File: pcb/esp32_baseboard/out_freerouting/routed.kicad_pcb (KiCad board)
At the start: 2 copper layers, 235 x 132 mm, 42 parts, among them J1 Screw_12V_IN, J10 LIM_MIN_NC, J11 LIM_MAX_NC, J12 LIM_MIN_NC, J13 LIM_MAX_NC, J14 BUP_30S, J15 BUZZER_5V, J16 AOD4184, J17 TFT_TOUCH, J18 EC11_ENC, J2 NEMA17_OUT, J4 OPTO_FIELD_IN, J5 GA12_N20, J6 GA12_N20, J7 GA12_N20, J8 LIM_MIN_NC, J9 LIM_MAX_NC, U1 ESP32_S3_DevKitC_1, U2 MP1584_5V3A, U3 TMC2209, U4 PC817_4CH, U5 DRV8871_Module, U6 DRV8871_Module, U7 DRV8871_Module, U9 PC817_4CH

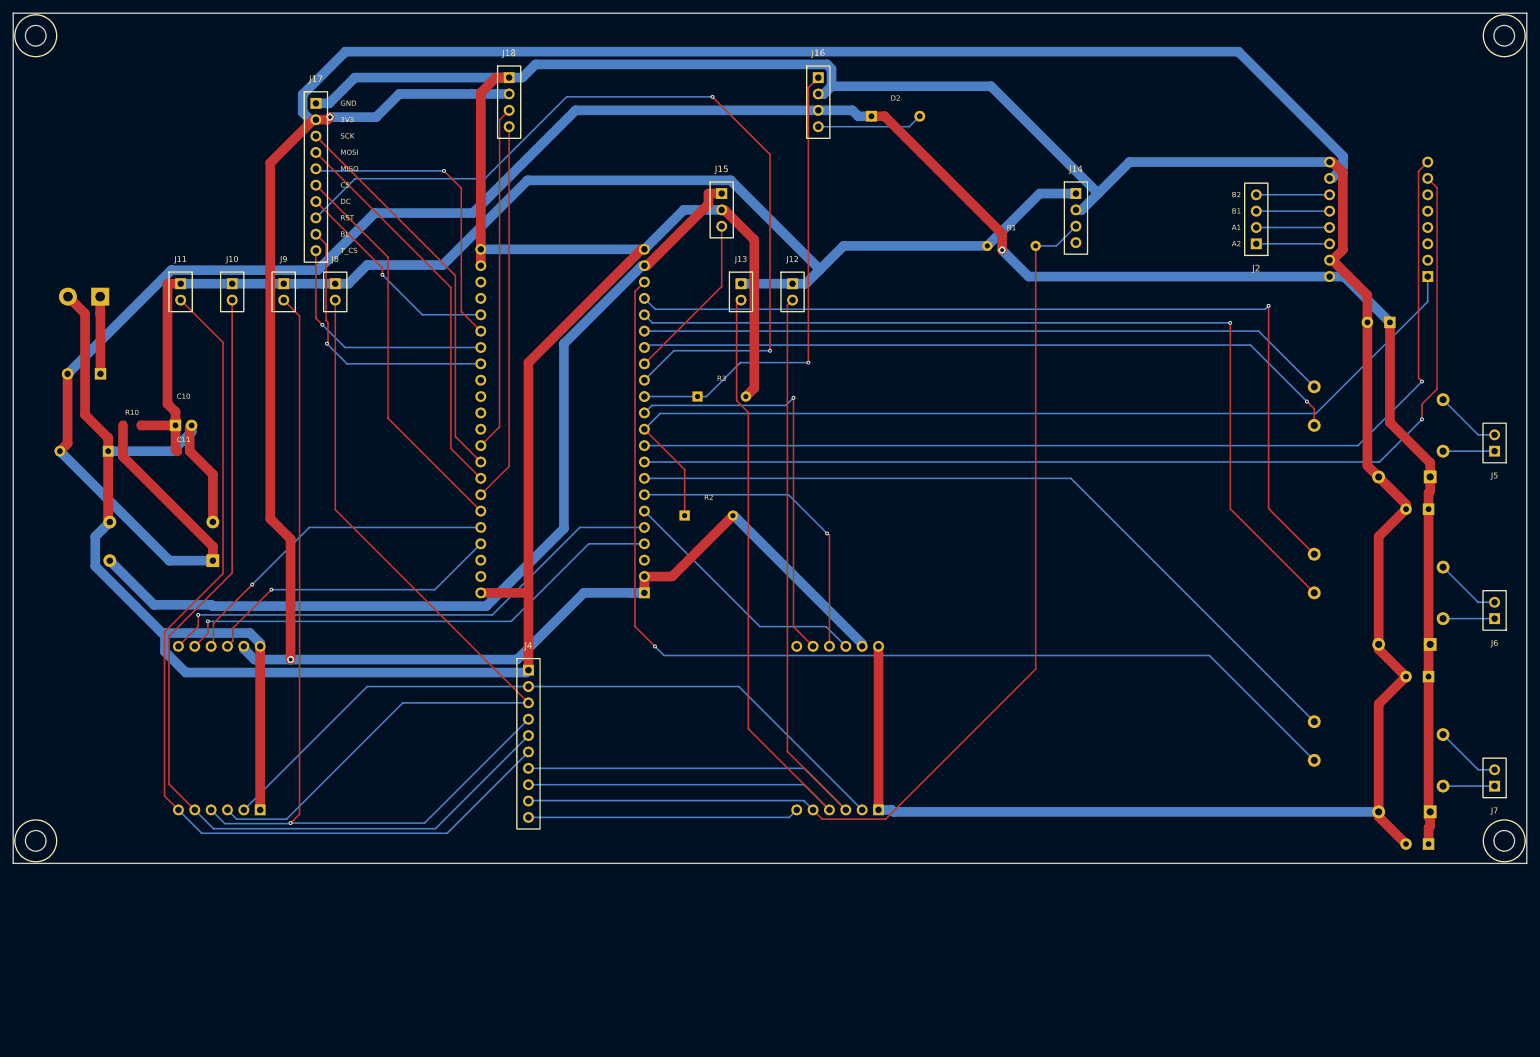
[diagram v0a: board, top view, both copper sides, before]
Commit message: sắp xếp và chọn lại linh kiện cho PCB
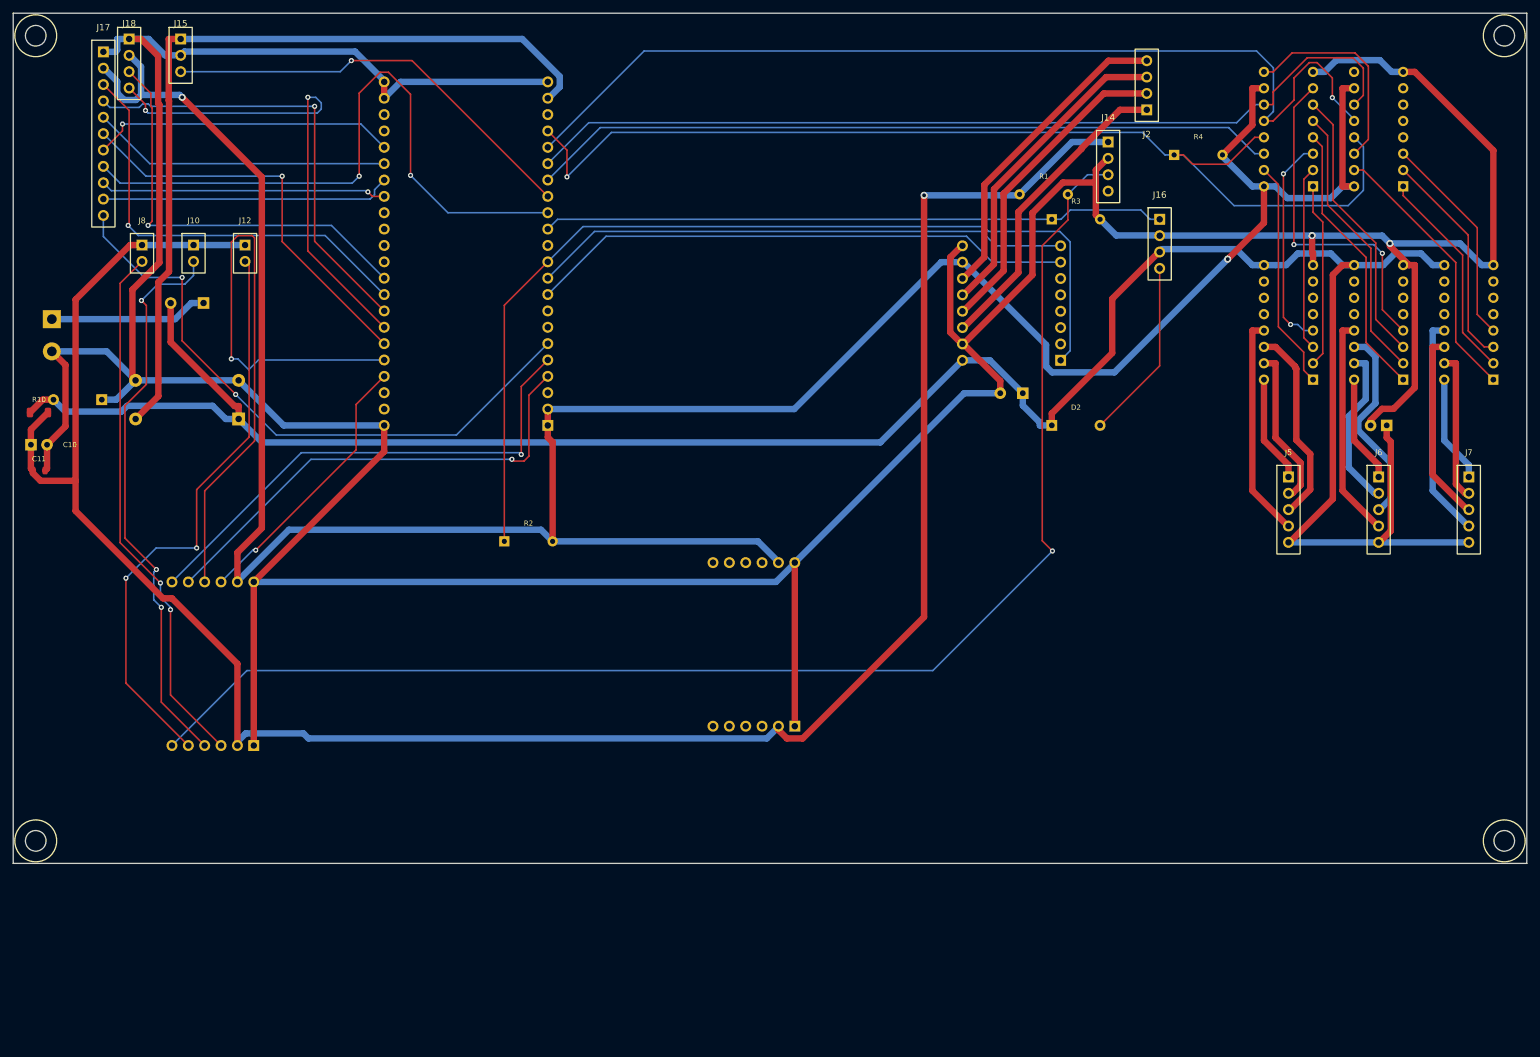
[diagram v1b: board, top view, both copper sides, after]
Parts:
- removed C22, C23: 470u/25V, ESP32_Carrier:CP_Radial_D8_470u_25V
- removed J11, J13, J9: LIM_MAX_NC, ESP32_Carrier:PinHeader_1x02_LimitSW
- removed J4: OPTO_FIELD_IN, ESP32_Carrier:PinHeader_1x10_OptoField
- added R4: 10k, ESP32_Carrier:R_Axial_4k7_BUP, F.Cu at (219.0, 52.0)
- added U10: 74HC595, ESP32_Carrier:74HC595, B.Cu at (233.0, 48.0)
- added U11: 74HC595, ESP32_Carrier:74HC595, B.Cu at (247.0, 48.0)
- C21: value 470u/25V -> 100u/25V; footprint ESP32_Carrier:CP_Radial_D8_470u_25V -> ESP32_Carrier:CP_Radial_D6_100u_25V
- J10: value LIM_MIN_NC -> LIM_HOME2
- J12: value LIM_MIN_NC -> LIM_HOME3
- J17: footprint ESP32_Carrier:PinHeader_1x10_TFT -> ESP32_Carrier:PinHeader_1x11_TFT
- J5, J6, J7: value GA12_N20 -> 28BYJ48; footprint ESP32_Carrier:PinHeader_1x02_MotorDC -> ESP32_Carrier:PinHeader_1x05_BYJ
- J8: value LIM_MIN_NC -> LIM_HOME1
- U5, U6, U7: value DRV8871_Module -> ULN2003AN; footprint ESP32_Carrier:DRV8871_Module -> ESP32_Carrier:ULN2003AN
- U9: value PC817_4CH -> PC817_4CH_DNP
- moved J15 87.4 mm to (61.0, 34.0)
- moved J12 85.2 mm to (71.0, 66.0)
- moved U7 69.4 mm to (261.0, 78.0)
- moved R3 61.5 mm to (200.0, 62.0)
- moved J18 59.3 mm to (53.0, 34.0)
- moved U3 58.5 mm to (190.0, 75.0)
- moved C20 58.1 mm to (190.0, 89.0)
- moved J16 57.4 mm to (213.0, 62.0)
- moved D2 55.6 mm to (200.0, 94.0)
- moved J7 48.2 mm to (261.0, 102.0), turned to 0 degrees
- moved U6 42.0 mm to (247.0, 78.0)
- moved J17 34.0 mm to (49.0, 36.0)
- moved J5 32.2 mm to (233.0, 102.0), turned to 0 degrees
- moved J8 30.6 mm to (55.0, 66.0)
- moved U1 30.0 mm to (118.0, 94.0)
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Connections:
- J10 pad 2: OPTO_IN3 -> OPTO_IN2
- J12 pad 2: OPTO_IN5 -> OPTO_IN3
- J14 pad 3: OPTO_IN7 -> OPTO_IN4
- J5 pad 1: MotDC1_A -> BYJ1_A
- J5 pad 2: MotDC1_B -> BYJ1_B
- J6 pad 1: MotDC2_A -> BYJ2_A
- J6 pad 2: MotDC2_B -> BYJ2_B
- J7 pad 1: MotDC3_A -> BYJ3_A
- J7 pad 2: MotDC3_B -> BYJ3_B
- R1 pad 2: OPTO_IN7 -> OPTO_IN4
- U1 pad 12: OPTO_OUT7 -> unconnected-(U1-IO8-Pad12)
- U1 pad 16: DC1_IN1 -> SER
- U1 pad 17: DC1_IN2 -> SRCLK
- U1 pad 18: DC2_IN1 -> RCLK
- U1 pad 19: DC2_IN2 -> OE_595
- U1 pad 20: DC3_IN1 -> unconnected-(U1-IO14-Pad20)
- U1 pad 6: OPTO_OUT5 -> T_IRQ
- U1 pad 7: OPTO_OUT6 -> unconnected-(U1-IO7-Pad7)
- U1 pad 8: DC3_IN2 -> unconnected-(U1-IO15-Pad8)
- U4 pad 2: OPTO_VCC_I -> +12V_SNS
- U5 pad 1: +12V -> SR_Q0
- U5 pad 2: GND -> SR_Q1
- U5 pad 3: DC1_IN1 -> SR_Q2
- U5 pad 4: DC1_IN2 -> SR_Q3
- U5 pad 5: MotDC1_A -> unconnected-(U5-IN5-Pad5)
- U5 pad 6: MotDC1_B -> unconnected-(U5-IN6-Pad6)
- U6 pad 1: +12V -> SR_Q4
- U6 pad 2: GND -> SR_Q5
- U6 pad 3: DC2_IN1 -> SR_Q6
- U6 pad 4: DC2_IN2 -> SR_Q7
- U6 pad 5: MotDC2_A -> unconnected-(U6-IN5-Pad5)
- U6 pad 6: MotDC2_B -> unconnected-(U6-IN6-Pad6)
- U7 pad 1: +12V -> SR_Q8
- U7 pad 2: GND -> SR_Q9
- U7 pad 3: DC3_IN1 -> SR_Q10
- U7 pad 4: DC3_IN2 -> SR_Q11
- U7 pad 5: MotDC3_A -> unconnected-(U7-IN5-Pad5)
- U7 pad 6: MotDC3_B -> unconnected-(U7-IN6-Pad6)
- U9 pad 10: OPTO_OUT6 -> unconnected-(U9-OUT2-Pad10)
- U9 pad 11: OPTO_OUT7 -> unconnected-(U9-OUT3-Pad11)
- U9 pad 12: OPTO_OUT8 -> unconnected-(U9-OUT4-Pad12)
- U9 pad 2: OPTO_VCC_I -> +12V_SNS
- U9 pad 3: OPTO_IN5 -> unconnected-(U9-IN1-Pad3)
- U9 pad 4: OPTO_IN6 -> unconnected-(U9-IN2-Pad4)
- U9 pad 5: OPTO_IN7 -> unconnected-(U9-IN3-Pad5)
- U9 pad 6: OPTO_IN8 -> unconnected-(U9-IN4-Pad6)
- U9 pad 9: OPTO_OUT5 -> unconnected-(U9-OUT1-Pad9)
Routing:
- net DC3_IN1: track 168.2 -> 0.00 mm, vias 1 -> 0
- net OE_595: track 0.00 -> 165.7 mm, vias 0 -> 1
- net OPTO_IN7: track 162.8 -> 0.00 mm
- net RCLK: track 0.00 -> 154.3 mm, vias 0 -> 1
- net SRCLK: track 0.00 -> 141.5 mm
- net +12V_SNS: track 203.5 -> 343.3 mm, vias 0 -> 1
- net DC2_IN2: track 139.3 -> 0.00 mm, vias 1 -> 0
- net DC2_IN1: track 138.8 -> 0.00 mm, vias 1 -> 0
- net OPTO_IN5: track 135.2 -> 0.00 mm
- net OPTO_IN6: track 133.8 -> 0.00 mm
- net DC3_IN2: track 119.6 -> 0.00 mm
- net GND: track 780.9 -> 661.3 mm, vias 0 -> 2
- net SER: track 0.00 -> 116.2 mm
- net OPTO_VCC_I: track 111.9 -> 0.00 mm
- net DC1_IN1: track 110.8 -> 0.00 mm, vias 1 -> 0
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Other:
- board text added: "1 POWER"
- board text added: "5 U10/11 + U5-7"
- board text added: "B STEP J2"
- board text added: "BOTTOM — POWER | MCU | TMC | OPTO | 595/ULN"
- board text added: "C HMI"
- board text added: "C20 470u/25V TMC"
- board text added: "C21 100u/25V ULN"
- board text added: "E BYJ J5-J7"
- board text added: "F HOME J8/10/12"
- board text added: "G BLW"
- board text added: "J10 HOME2"
- board text added: "J12 HOME3"
- board text added: "J5 28BYJ BYJ1"
- board text added: "J6 28BYJ BYJ2"
- board text added: "J7 28BYJ BYJ3"
- board text added: "J8 HOME1"
- board text added: "R4 OE_595 pull-up 10k"
- board text added: "TOP 235x132 — ULN/595 + HOME + BYJ"
- board text added: "U10 74HC595"
- board text added: "U11 74HC595"
- board text added: "U4 used | U9 DNP spare"
- board text added: "U5 ULN2003AN"
- board text added: "U6 ULN2003AN"
- board text added: "U7 ULN2003AN"
- board text added: "U9 PC817 4CH DNP"
- board text removed: "1 POWER J1/F1/D1/U2"
- board text removed: "2x PC817 4CH | OUT=MCU IN=J4 field"
- board text removed: "5 DRV U5-U7"
- board text removed: "B STEP J2 -> U3"
- board text removed: "BOTTOM — 1 POWER | 2 MCU | 3 TMC | 4 OPTO | 5 DRV"
- board text removed: "C HMI J17/J18/J15"
- board text removed: "C20 470u TMC"
- board text removed: "C21 470u U5"
- board text removed: "C22 470u U6"
- board text removed: "C23 470u U7"
- board text removed: "D FIELD J4"
- board text removed: "E DC MOT J5-J7"
- board text removed: "F LIMIT truc 1-2 (-> U4)"
- board text removed: "F LIMIT truc 3 (-> U9)"
- board text removed: "G BLW J16"
- board text removed: "IN1-6=lim; IN7=BUP30S; IN8 free"
- board text removed: "J4 OPTO FIELD IN"
- board text removed: "J5 GA12-N20 TRUC1"
- board text removed: "J6 GA12-N20 TRUC2"
- board text removed: "J7 GA12-N20 TRUC3"
- board text removed: "T1 J8 MIN"
- board text removed: "T1 J9 MAX"
- board text removed: "T2 J10 MIN"
- board text removed: "T2 J11 MAX"
- board text removed: "T3 J12 MIN"
- board text removed: "T3 J13 MAX"
- board text removed: "TOP 235x132 — giac canh module dieu khien no"
- board text removed: "U5 DRV8871 GA12 VM=12V"
- board text removed: "U6 DRV8871 GA12 VM=12V"
- board text removed: "U7 DRV8871 GA12 VM=12V"
- board text removed: "U9 PC817 4CH"

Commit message: đi dây cho mạch PCB
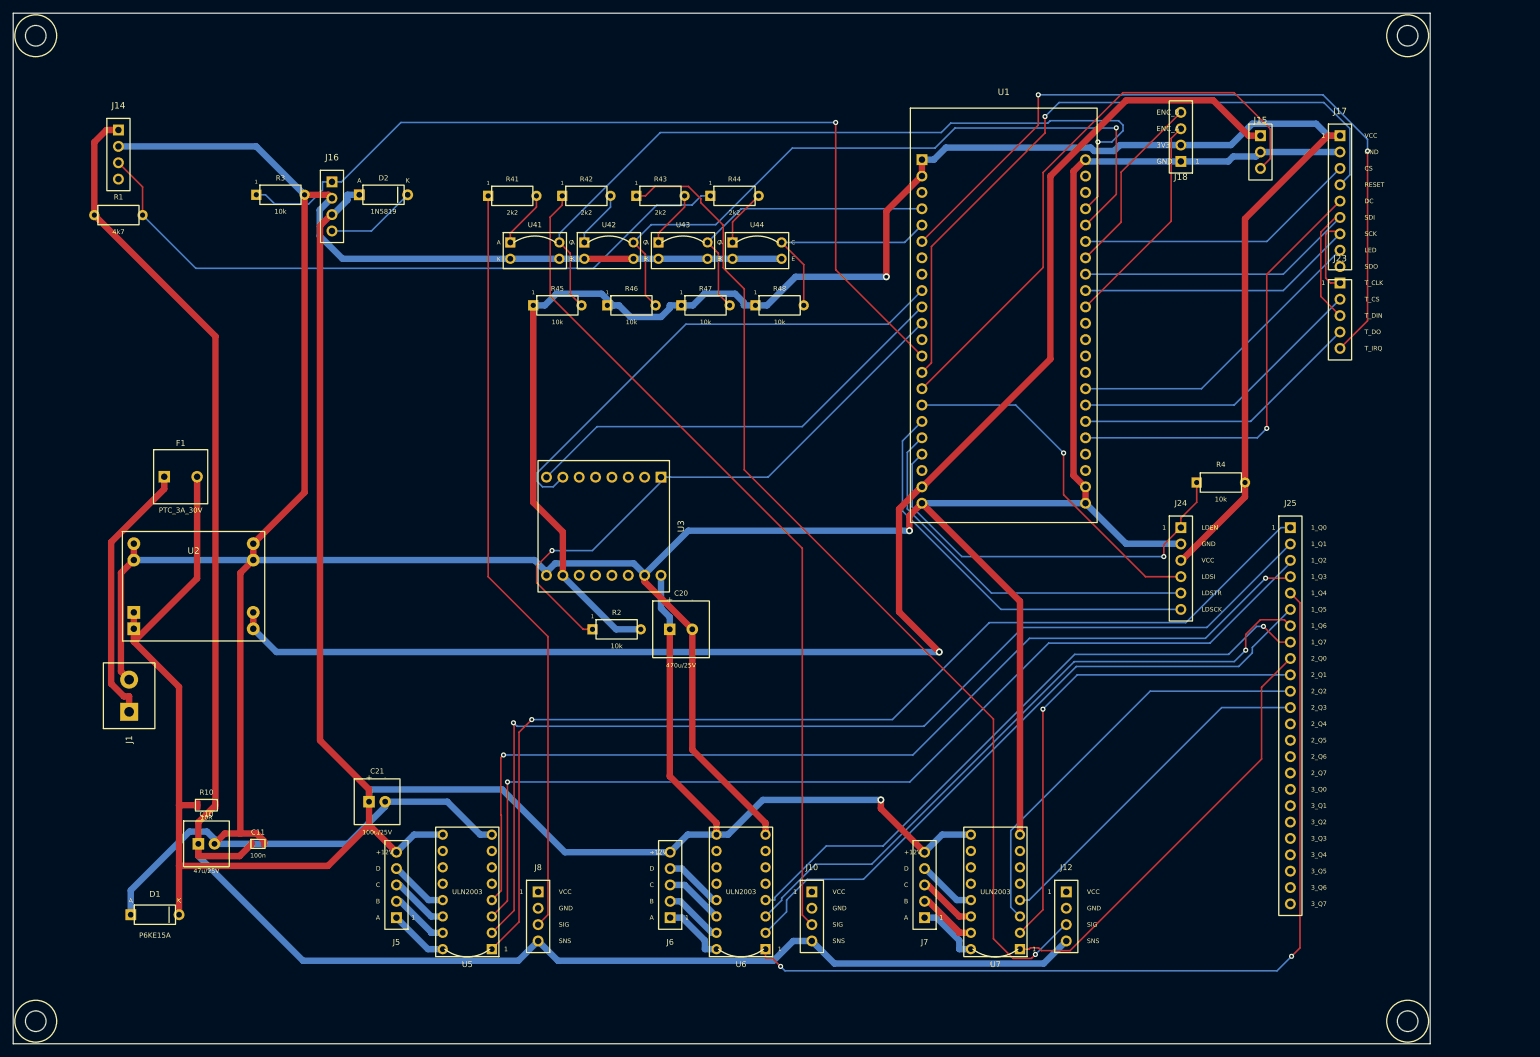
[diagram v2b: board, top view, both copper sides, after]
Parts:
- removed J2: NEMA17_OUT, ESP32_Carrier:PinHeader_1x04_Motor
- removed U10, U11: 74HC595, ESP32_Carrier:74HC595
- removed U4: PC817_4CH, ESP32_Carrier:PC817_4CH_Opto
- removed U9: PC817_4CH_DNP, ESP32_Carrier:PC817_4CH_Opto
- added J23: TFT_TP, ESP32_Carrier:PinHeader_1x05_TFT_TP, F.Cu at (241.0, 71.9)
- added J24: 595_CTRL, ESP32_Carrier:PinHeader_1x06_595CTRL, F.Cu at (216.3, 109.9)
- added J25: 595_Q, ESP32_Carrier:PinHeader_1x24_595Q, F.Cu at (233.3, 109.9)
- added R41: 2k2, ESP32_Carrier:R_Axial_4k7_BUP, F.Cu at (112.5, 58.4)
- added R42: 2k2, ESP32_Carrier:R_Axial_4k7_BUP, F.Cu at (124.0, 58.4)
- added R43: 2k2, ESP32_Carrier:R_Axial_4k7_BUP, F.Cu at (135.5, 58.4)
- added R44: 2k2, ESP32_Carrier:R_Axial_4k7_BUP, F.Cu at (147.0, 58.4)
- added R45: 10k, ESP32_Carrier:R_Axial_4k7_BUP, F.Cu at (119.5, 75.4)
- added R46: 10k, ESP32_Carrier:R_Axial_4k7_BUP, F.Cu at (131.0, 75.4)
- added R47: 10k, ESP32_Carrier:R_Axial_4k7_BUP, F.Cu at (142.5, 75.4)
- added R48: 10k, ESP32_Carrier:R_Axial_4k7_BUP, F.Cu at (154.0, 75.4)
- added U41: PC817, ESP32_Carrier:PC817_DIP4, F.Cu at (116.0, 66.9)
- added U42: PC817, ESP32_Carrier:PC817_DIP4, F.Cu at (127.5, 66.9)
- added U43: PC817, ESP32_Carrier:PC817_DIP4, F.Cu at (139.0, 66.9)
- added U44: PC817, ESP32_Carrier:PC817_DIP4, F.Cu at (150.5, 66.9)
- C20, C21, D1, F1, J1, U1, U2, U3, U5, U6, U7: moved to F.Cu
- J10: value LIM_HOME2 -> END_HOME2; footprint ESP32_Carrier:PinHeader_1x02_LimitSW -> ESP32_Carrier:PinHeader_1x04_Endstop
- J12: value LIM_HOME3 -> END_HOME3; footprint ESP32_Carrier:PinHeader_1x02_LimitSW -> ESP32_Carrier:PinHeader_1x04_Endstop
- J17: value TFT_TOUCH -> TFT_LCD; footprint ESP32_Carrier:PinHeader_1x11_TFT -> ESP32_Carrier:PinHeader_1x09_TFT_LCD
- J8: value LIM_HOME1 -> END_HOME1; footprint ESP32_Carrier:PinHeader_1x02_LimitSW -> ESP32_Carrier:PinHeader_1x04_Endstop
- moved J17 192.4 mm to (241.0, 49.0)
- moved J15 168.3 mm to (228.6, 49.0)
- moved C21 166.1 mm to (91.5, 152.4), turned to 0 degrees
- moved J18 164.4 mm to (216.3, 53.0), turned to 180 degrees
- moved J12 162.3 mm to (198.5, 166.4)
- moved U5 155.2 mm to (105.5, 166.4)
- moved J5 154.5 mm to (94.5, 170.4), turned to 180 degrees
- moved J14 153.7 mm to (51.3, 48.1)
- moved R1 143.7 mm to (51.3, 61.3)
- moved J10 138.9 mm to (159.0, 166.4)
- moved U6 132.7 mm to (148.0, 166.4)
- moved J6 129.5 mm to (137.0, 170.4), turned to 180 degrees
- moved J16 128.6 mm to (84.5, 56.2)
- moved R3 123.6 mm to (76.5, 58.2)
- moved J8 117.8 mm to (116.5, 166.4)
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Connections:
- J10 pad 1: +12V_SNS -> unconnected-(J10-VCC-Pad1)
- J10 pad 2: OPTO_IN2 -> unconnected-(J10-GND-Pad2)
- J12 pad 1: +12V_SNS -> unconnected-(J12-VCC-Pad1)
- J12 pad 2: OPTO_IN3 -> unconnected-(J12-GND-Pad2)
- J17 pad 1: GND -> +3V3
- J17 pad 2: +3V3 -> GND
- J17 pad 3: TFT_SCK -> TFT_CS
- J17 pad 4: TFT_MOSI -> TFT_RST
- J17 pad 5: TFT_MISO -> TFT_DC
- J17 pad 6: TFT_CS -> TFT_MOSI
- J17 pad 7: TFT_DC -> TFT_SCK
- J17 pad 8: TFT_RST -> TFT_BL
- J17 pad 9: TFT_BL -> unconnected-(J17-SDO-Pad9)
- J8 pad 1: +12V_SNS -> unconnected-(J8-VCC-Pad1)
- J8 pad 2: OPTO_IN1 -> unconnected-(J8-GND-Pad2)
- U2 pad 3: +5V -> GND
- U2 pad 4: GND -> +5V
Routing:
- net SR_Q1: track 28.7 -> 166.6 mm, vias 0 -> 1
- net SR_Q0: track 35.7 -> 168.3 mm, vias 0 -> 1
- net SR_Q2: track 28.6 -> 157.9 mm, vias 0 -> 1
- net +3V3: track 417.1 -> 288.3 mm, vias 2 -> 1
- net SR_Q3: track 33.6 -> 157.0 mm
- net OPTO_IN4: track 214.4 -> 105.9 mm, vias 1 -> 0
- net +5V: track 128.5 -> 236.6 mm, vias 0 -> 1
- net OE_595: track 165.7 -> 64.7 mm
- net SR_Q4: track 43.4 -> 142.4 mm, vias 0 -> 2
- net RCLK: track 154.3 -> 59.9 mm, vias 1 -> 0
- net OPTO_OUT1: track 42.7 -> 124.3 mm
- net SRCLK: track 141.5 -> 64.7 mm
- net OPTO_IN3: track 91.0 -> 159.9 mm, vias 2 -> 1
- net SER: track 116.2 -> 55.0 mm, vias 0 -> 1
- net SR_Q5: track 43.4 -> 103.8 mm
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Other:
- board size 235 x 132 mm -> 220 x 160 mm
- board text added: "1: POWER J1+F1+D1+U2+RC"
- board text added: "2: MCU U1 ESP32-S3 DevKitC"
- board text added: "3: TMC U3 + Mot pins (NEMA17 on module)"
- board text added: "4: OPTO U41-U44 PC817 + R2k2/10k"
- board text added: "5: SHIFT U10 595-24IO + J24/J25 + R4"
- board text added: "A1: HOME1+U5+J5"
- board text added: "A2: HOME2+U6+J6"
- board text added: "A3: HOME3+U7+J7"
- board text added: "All parts TOP (F.Cu); B.Cu = routing only. Eco1 cluster = cyan"
- board text added: "B: BLOWER J16 AOD4184 + R3/D2"
- board text added: "C: HMI J17 LCD + J23 TP + J18 ENC + J15 BZ"
- board text added: "LCD"
- board text added: "OPTO PC817x8 + 2k2/10k"
- board text added: "R4 LDEN/OE pull-up 10k"
- board text added: "R41 LED HOME1"
- board text added: "R42 LED HOME2"
- board text added: "R43 LED HOME3"
- board text added: "R44 LED BUP"
- board text added: "R45 PU HOME1"
- board text added: "R46 PU HOME2"
- board text added: "R47 PU HOME3"
- board text added: "R48 PU BUP"
- board text added: "Shopee thegioimodule 3x595"
- board text added: "TP"
- board text added: "U10 74HC595-24IO module"
- board text added: "U: BUP-30S J14 + R1 4k7"
- board text removed: "1 POWER"
- board text removed: "2 MCU U1"
- board text removed: "3 TMC U3"
- board text removed: "5 U10/11 + U5-7"
- board text removed: "B STEP J2"
- board text removed: "BOTTOM — POWER | MCU | TMC | OPTO | 595/ULN"
- board text removed: "C HMI"
- board text removed: "E BYJ J5-J7"
- board text removed: "F HOME J8/10/12"
- board text removed: "G BLW"
- board text removed: "R4 OE_595 pull-up 10k"
- board text removed: "TOP 235x132 — ULN/595 + HOME + BYJ"
- board text removed: "U10 74HC595"
- board text removed: "U11 74HC595"
- board text removed: "U4 PC817 4CH"
- board text removed: "U4 used | U9 DNP spare"
- board text removed: "U5 ULN2003AN"
- board text removed: "U6 ULN2003AN"
- board text removed: "U7 ULN2003AN"
- board text removed: "U9 PC817 4CH DNP"
